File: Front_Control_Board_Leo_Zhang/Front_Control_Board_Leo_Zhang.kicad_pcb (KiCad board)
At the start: 2 copper layers, 110 parts, among them J1 22035035, J10 430450200, J11 430450200, J12 430450200, J13 22035035, J14 M22-7130442, J2 Molex Micro-Fit 4 Pin, J3 430450200, J4 430450200, J5 430450200, J6 430450200, J7 22035035, J8 22035035, J9 22035035, Q1 PSMN5R2-60YL, Q2 PSMN5R2-60YL, Q3 PSMN5R2-60YL, Q4 PSMN5R2-60YL, Q5 PSMN5R2-60YL, Q6 PSMN5R2-60YL, U2 ADS1118IDGS, U3 MCP2562-E-P, U4 MCP6286T-E/OT, U5 UA78M05QDCYRG4Q1, U6 MCP6286T-E/OT, U7 MCP6286T-E/OT

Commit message: Done w first draft! waiting for feedback
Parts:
- removed D2, D3: PTVS12VZ1USK, Diode_SMD:Nexperia_DSN1608-2_1.6x0.8mm
- added J15: M22-7130442, SMV_Connectors:M22-7130442_TYC, F.Cu at (247.5, 45.0)
- added TP37: BlinkRSig, TestPoint:TestPoint_Pad_D1.0mm, F.Cu at (249.5, 67.8)
- added TP38: HLRSig, TestPoint:TestPoint_Pad_D1.0mm, F.Cu at (250.0, 61.2)
- added TP39: HLLSig, TestPoint:TestPoint_Pad_D1.0mm, F.Cu at (251.5, 55.0)
- added TP40: HornSig, TestPoint:TestPoint_Pad_D1.0mm, F.Cu at (247.8, 56.2)
- J14: footprint Jumperz:M22-7130442_TYC -> SMV_Connectors:M22-7130442_TYC
- TP1: value TestPoint -> BlinkLSig
- TP16: value BlinkR_MOS_G -> BlinkL_MOS_G
- TP17: value Pressure -> Accelerator
- TP7: value Pressure -> Brake
- U3: footprint Package_DIP:DIP-8_W7.62mm -> Package_DIP:SMDIP-8_W7.62mm
- moved J6 243.4 mm to (273.8, 105.4)
- moved J3 203.6 mm to (270.5, 22.2), turned to 90 degrees
- moved J5 196.9 mm to (151.0, 27.3), turned to 180 degrees
- moved J4 182.0 mm to (270.2, 48.5), turned to 90 degrees
- moved J12 154.5 mm to (270.2, 34.5), turned to 90 degrees
- moved J10 153.2 mm to (270.2, 72.0), turned to 90 degrees
- moved J11 144.8 mm to (270.2, 60.0), turned to 90 degrees
- moved U1 127.3 mm to (210.6, 59.2)
- moved TP12 126.6 mm to (259.5, 19.5), turned to -90 degrees
- moved Q1 125.9 mm to (261.6, 24.6), turned to -90 degrees
- moved Q4 125.0 mm to (260.4, 36.5), turned to -90 degrees
- moved J14 122.4 mm to (230.0, 102.9)
- moved TP22 121.0 mm to (265.2, 20.2), turned to 180 degrees
- moved Q5 119.7 mm to (260.3, 50.5), turned to -90 degrees
- moved TP4 117.0 mm to (257.8, 26.8), turned to -90 degrees
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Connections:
- J14 pad 1: (no net) -> /CAN_RX/Jump
- J14 pad 2: (no net) -> unconnected-(J14-A2-Pad2)
- J14 pad 3: (no net) -> unconnected-(J14-A3-Pad3)
- J14 pad 4: (no net) -> /CAN_TX/Jump
- R20 pad 2: Net-(U1-CN7_33) -> Net-(U1-VBAT)
- TP1 pad 1: unconnected-(TP1-Pad1) -> /BlinkLeft/STM32
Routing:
- net +3V3: track 0.00 -> 185.3 mm
- net /Pressure/VFin: track 0.00 -> 124.4 mm
- net /Brake(Hall)/VFin: track 0.00 -> 93.8 mm
- net /Accelerator(Hall)/VFin: track 0.00 -> 63.2 mm
- net GND: track 0.00 -> 62.0 mm, vias 0 -> 26
- net +5V: track 0.00 -> 53.7 mm
- net /Horn/STM32: track 0.00 -> 48.9 mm
- net /CANH: track 0.00 -> 41.6 mm
- net /CANL: track 0.00 -> 41.5 mm
- net /HLL/STM32: track 0.00 -> 39.7 mm
- net /PA8_D7_Standby: track 0.00 -> 37.6 mm
- net /Brake(Hall)/VFout: track 0.00 -> 30.9 mm
- net /D0/Wiper4: track 0.00 -> 30.0 mm
- net /Accelerator(Hall)/VFout: track 0.00 -> 29.8 mm
- net /HLR/STM32: track 0.00 -> 29.6 mm
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- added copper zone on F.Cu, net +12V
- added copper zone on F.Cu, net +5V
- added copper zone on B.Cu, net GND
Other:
- board outline added: 136.5 x 105.5 mm
- board text added: "BlinkL"
- board text added: "BlinkR"
- board text added: "HLL"
- board text added: "HLR"
- board text added: "Horn"
- board text added: "Wiper"

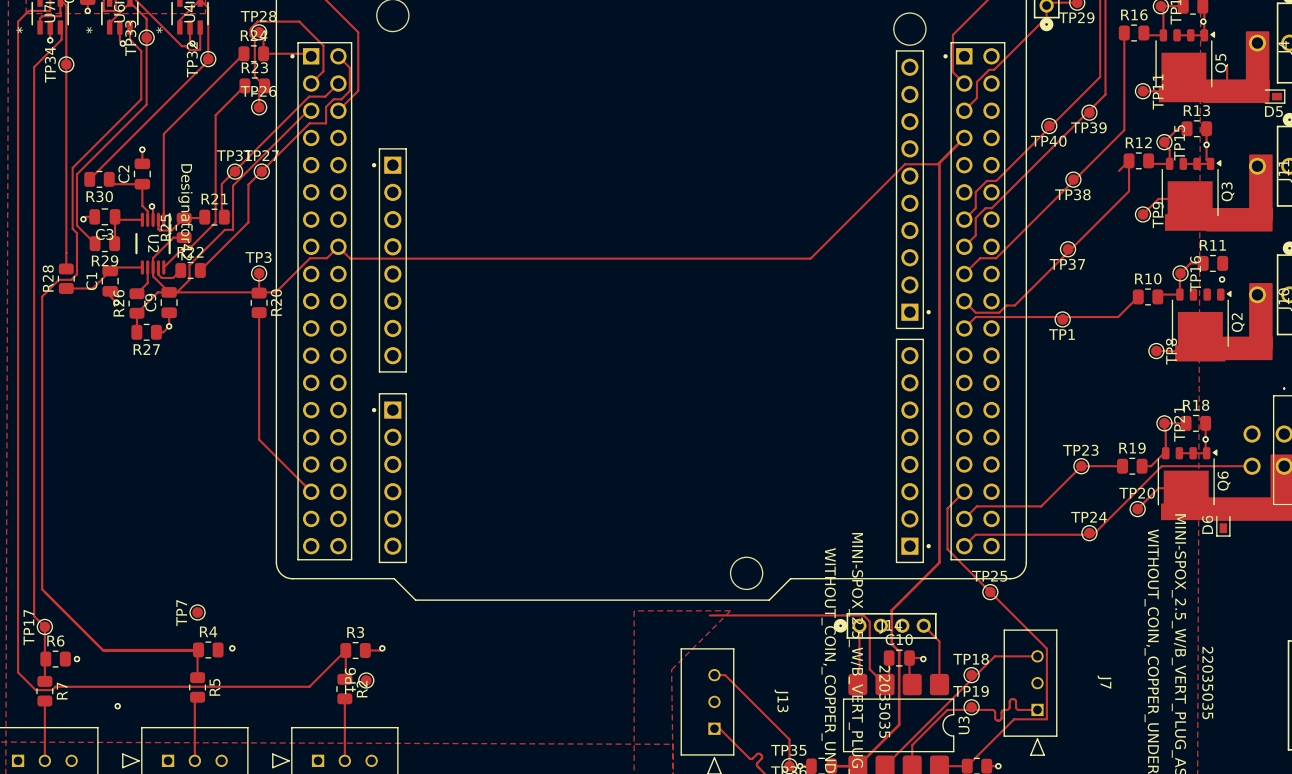
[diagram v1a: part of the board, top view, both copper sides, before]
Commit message: fixed some minor things, unconnected vias and test points
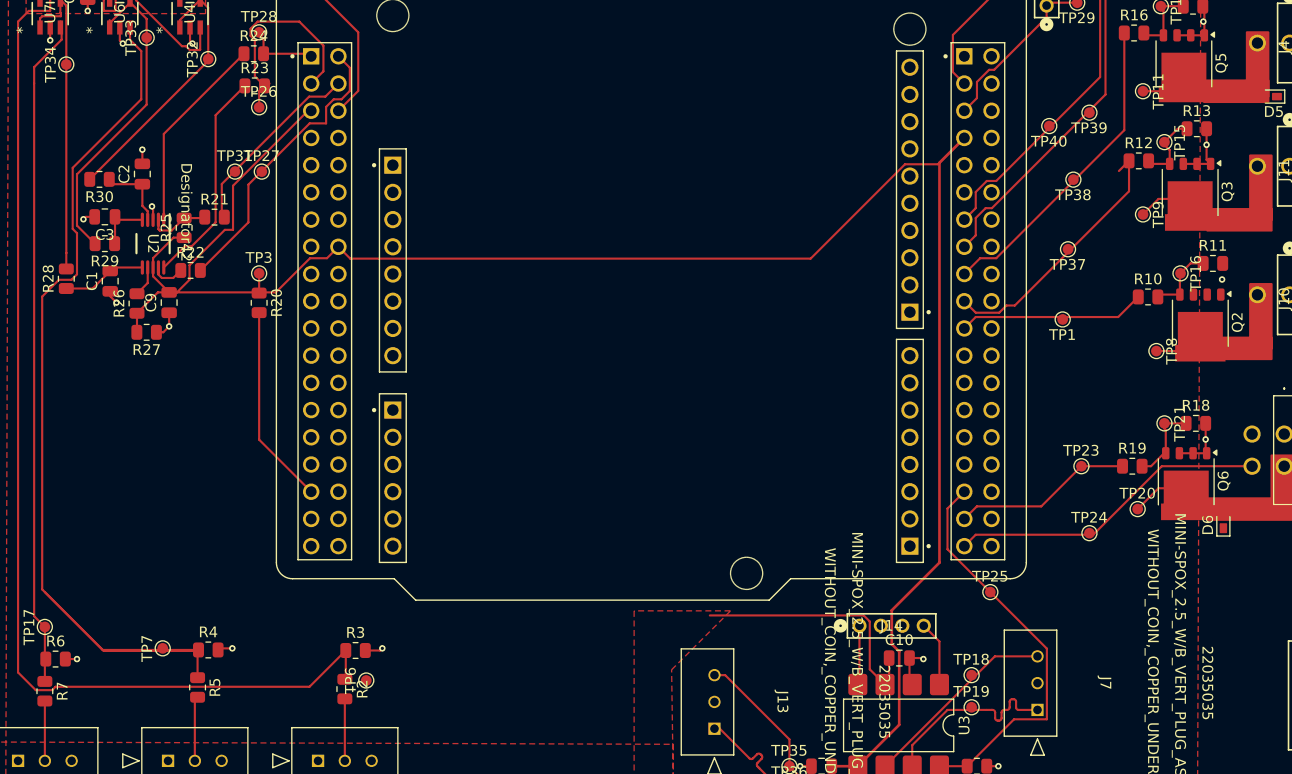
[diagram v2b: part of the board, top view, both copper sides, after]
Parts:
- moved TP7 4.67 mm to (165.0, 105.0)
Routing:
- net GND: track 62.0 -> 64.5 mm, vias 26 -> 25
- net Net-(D5-A): track 7.68 -> 5.78 mm
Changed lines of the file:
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@@
 	(footprint "TestPoint:TestPoint_Pad_D1.0mm"
 		(layer "F.Cu")
-		(at 168.25401 101.649998 90)
+		(at 165 105 90)
 		(descr "SMD pad as test Point, diameter 1.0mm")
 		(tags "test point SMD pad")
@@
 	)
 	(segment
+		(start 171.5 105)
+		(end 170.316508 105)
+		(width 0.2)
+		(layer "F.Cu")
+		(net 1)
+	)
+	(segment
 		(start 163.95 38.05)
 		(end 164.5 37.5)
@@
 	)
 	(segment
+		(start 157 106)
+		(end 155.9125 106)
+		(width 0.2)
+		(layer "F.Cu")
+		(net 1)
+	)
+	(segment
 		(start 262.3459 86.6911)
 		(end 262.4434 86.7886)
@@
 	)
 	(segment
+		(start 170.316508 105)
+		(end 170.16651 105.149998)
+		(width 0.2)
+		(layer "F.Cu")
+		(net 1)
+	)
+	(segment
 		(start 154.5 47.05)
 		(end 154.5 48.25)
@@
 	)
 	(via
-		(at 160.8 110.4)
-		(size 0.6)
-		(drill 0.3)
-		(layers "F.Cu" "B.Cu")
-		(free yes)
-		(net 1)
-	)
-	(via
 		(at 157 106)
 		(size 0.6)
@@
 	)
 	(segment
-		(start 264.350052 50.5834)
-		(end 264.350052 52.4834)
-		(width 0.2)
-		(layer "F.Cu")
-		(net 10)
-	)
-	(segment
 		(start 258.366652 53)
 		(end 256.5 53)
@@
 		(polygon
 			(pts
-				(xy 144.5 16.5) (xy 283 16) (xy 283 36.75) (xy 144.5 37) (xy 144.5 16.5)
+				(xy 144.5 16.5) (xy 283 16) (xy 283 36.75) (xy 144.5 37)
 			)
 		)

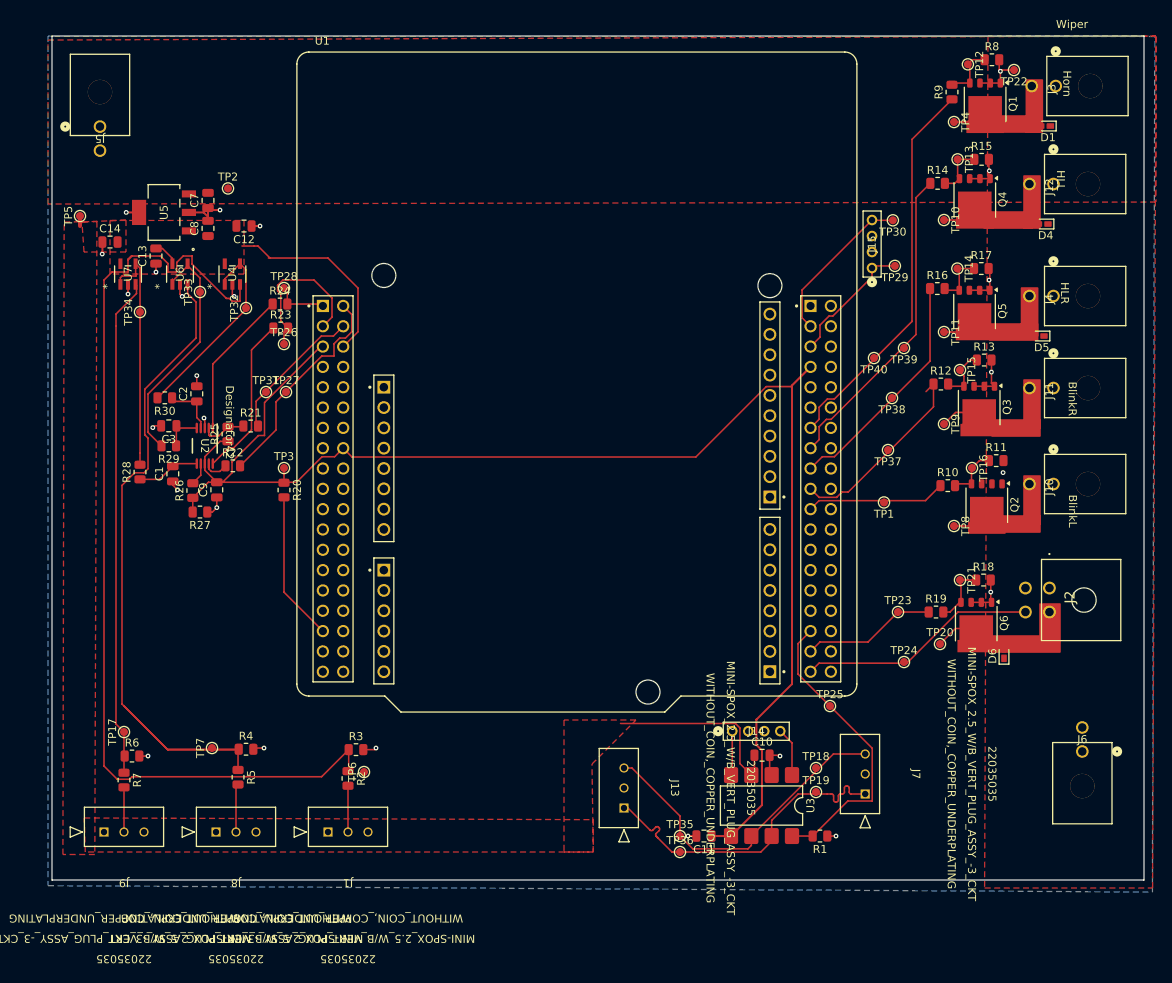
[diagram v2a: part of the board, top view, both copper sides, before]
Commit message: LEDs added, mosfet ground polygons, Ground plane, slight rerouting
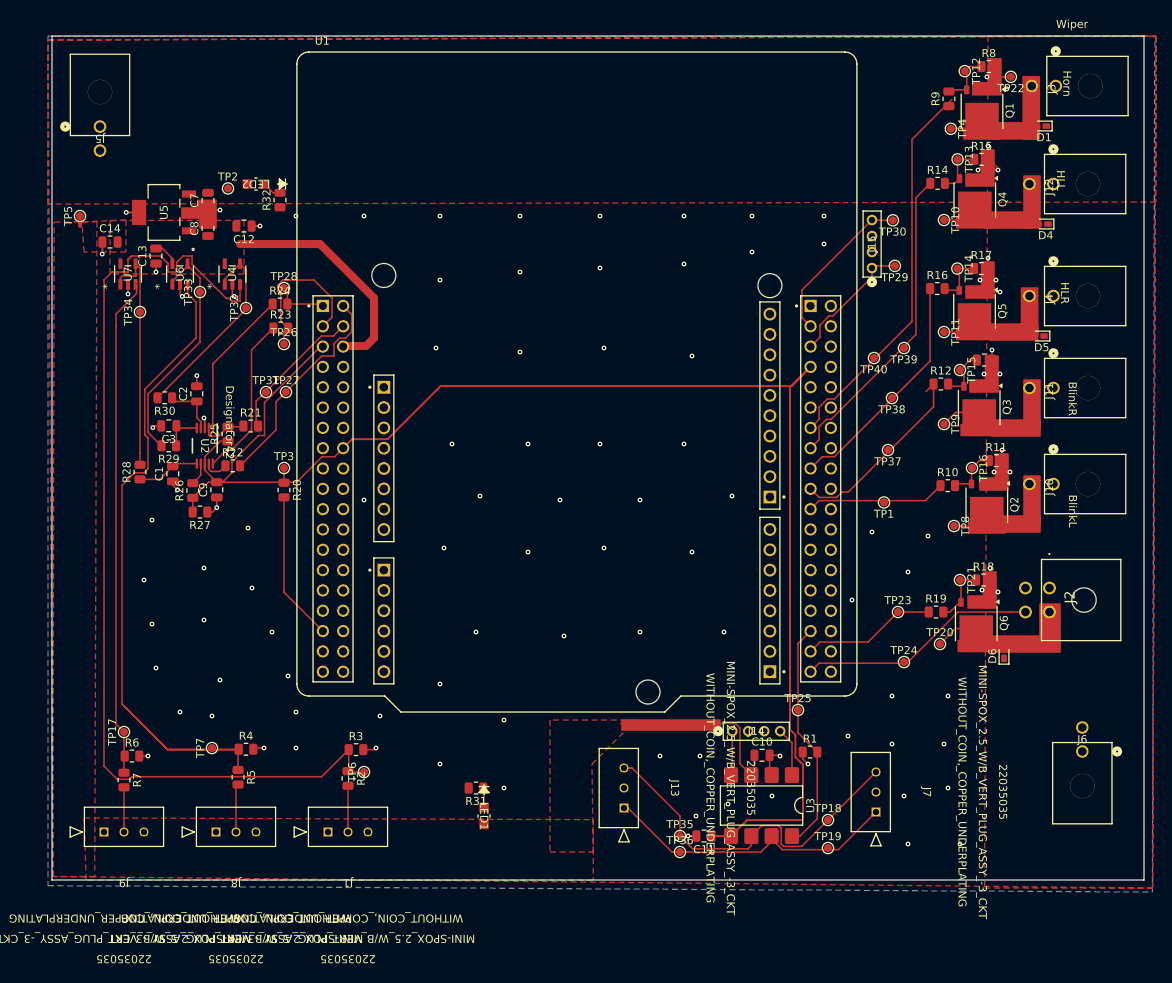
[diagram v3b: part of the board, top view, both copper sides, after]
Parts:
- added LED1: LTST-C170GKT, SMV_Passives:LED_LTST-C170GKT_LTO, F.Cu at (199.0, 113.5)
- added LED2: LTST-C170GKT, SMV_Passives:LED_LTST-C170GKT_LTO, F.Cu at (170.5, 34.5)
- added R31: 200, Resistor_SMD:R_0805_2012Metric, F.Cu at (198.0, 110.0)
- added R32: 1K, Resistor_SMD:R_0805_2012Metric, F.Cu at (173.5, 36.5)
- moved R1 10.6 mm to (239.8, 105.5), turned to 0 degrees
- moved TP19 7.16 mm to (242.0, 117.5)
- moved TP18 6.67 mm to (242.0, 114.0)
- moved TP25 4.03 mm to (238.2, 100.2)
- moved J7 2.63 mm to (248.0, 113.0)
- moved R8 0.93 mm to (262.1, 19.8)
- moved R9 0.93 mm to (257.1, 23.9)
- moved TP22 0.93 mm to (264.9, 21.1)
- moved TP4 0.93 mm to (257.4, 27.6)
- moved Q1 0.93 mm to (261.2, 25.4)
- moved TP12 0.93 mm to (259.1, 20.4)
- moved D1 0.50 mm to (269.0, 27.2)
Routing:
- net GND: track 64.5 -> 91.8 mm, vias 25 -> 110
- net /PA8_D7_Standby: track 37.6 -> 29.2 mm
- net +3V3: track 185.3 -> 189.3 mm
- net +5V: track 53.7 -> 57.6 mm
- net /CANH: track 41.6 -> 37.8 mm
- net /CANL: track 41.5 -> 45.2 mm
- net Net-(LED1-Pad1): track 0.00 -> 2.48 mm
- net Net-(LED2-Pad1): track 0.00 -> 2.40 mm
- net /Pressure/VFin: track 124.4 -> 126.5 mm
- added copper zone on F.Cu, net GND

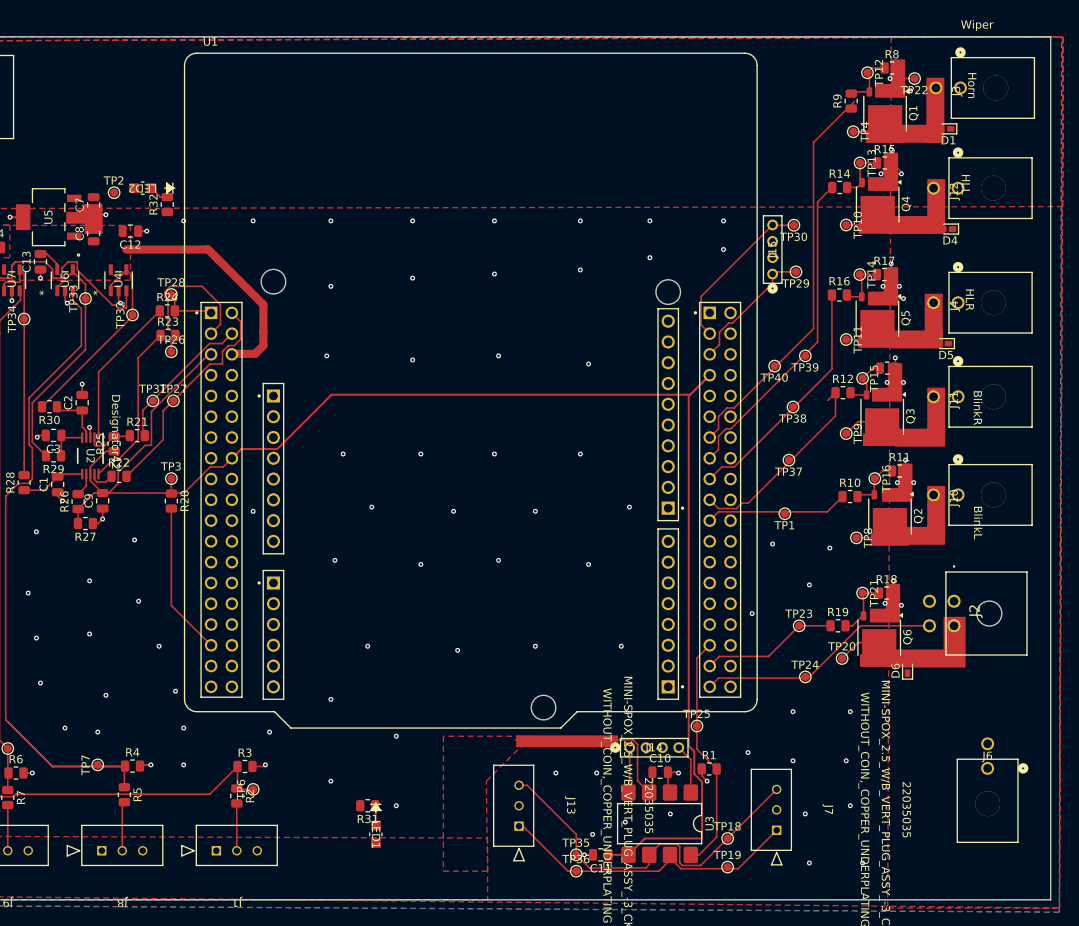
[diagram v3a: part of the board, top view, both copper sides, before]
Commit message: widened 12V plane connect
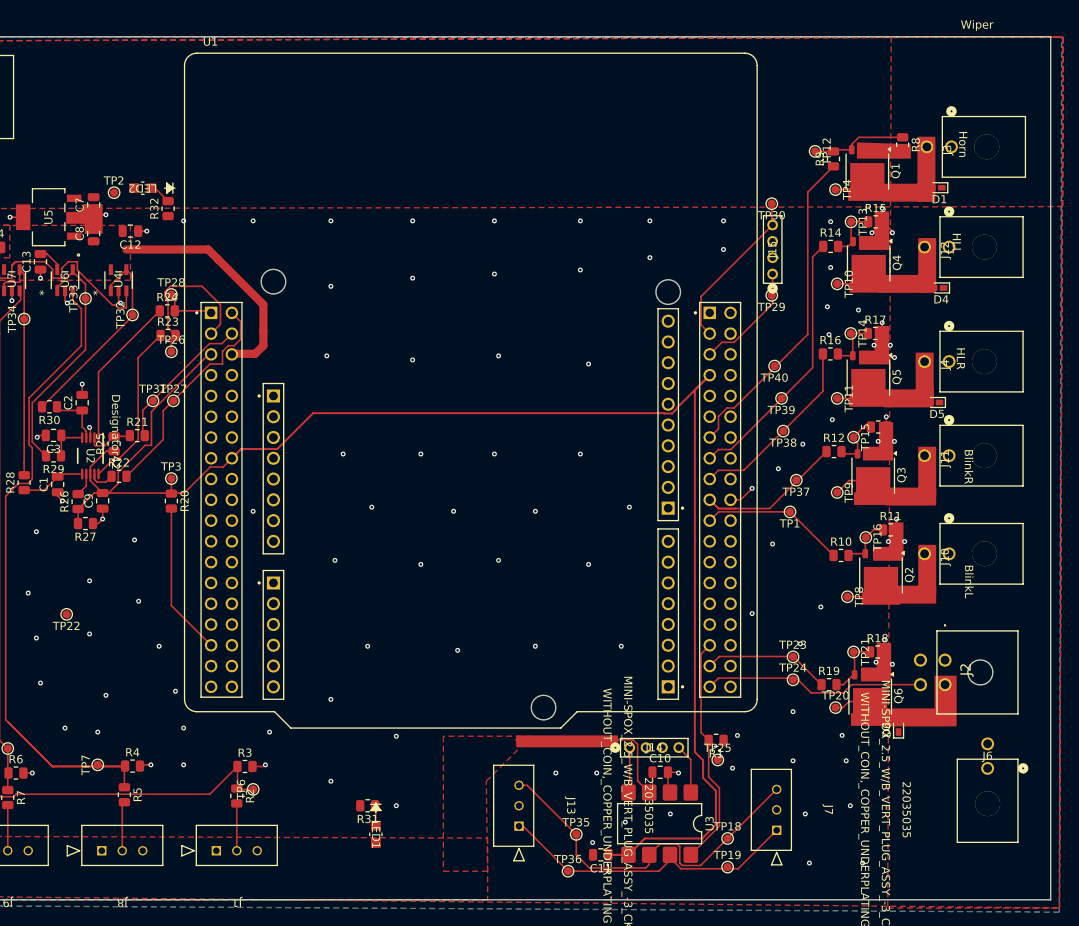
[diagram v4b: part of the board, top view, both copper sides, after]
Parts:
- moved TP22 122.6 mm to (161.2, 86.6)
- moved TP12 11.5 mm to (252.7, 30.0)
- moved R8 9.48 mm to (263.4, 29.2), turned to -90 degrees
- moved Q1 7.40 mm to (259.1, 32.5)
- moved R9 7.40 mm to (254.9, 30.9)
- moved TP4 7.40 mm to (255.2, 34.7)
- moved D1 7.28 mm to (267.9, 34.5)
- moved D6 7.28 mm to (262.9, 100.7)
- moved J10 7.28 mm to (269.1, 79.2)
- moved J11 7.28 mm to (269.1, 67.2)
- moved J12 7.28 mm to (269.1, 41.7)
- moved J2 7.28 mm to (268.6, 92.2)
- moved J4 7.28 mm to (269.1, 55.7)
- moved Q4 7.28 mm to (259.2, 43.7)
- moved R10 7.28 mm to (255.9, 79.4)
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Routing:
- net GND: track 91.8 -> 82.1 mm, vias 110 -> 116
- net /Horn/STM32: track 48.9 -> 39.9 mm
- net /HLL/STM32: track 39.7 -> 32.5 mm
- net /HLR/STM32: track 29.6 -> 22.8 mm
- net Net-(Q1-G): track 7.16 -> 11.9 mm
- net /BlinkRight/STM32: track 24.7 -> 21.3 mm
- net /D0/Wiper4: track 30.0 -> 27.4 mm
- net /CAN_TX: track 16.2 -> 14.3 mm
- net /D1/Wiper2: track 16.8 -> 15.6 mm
- net +3V3: track 189.3 -> 190.1 mm
- net Net-(D6-A): track 6.70 -> 5.91 mm
- net /PA8_D7_Standby: track 29.2 -> 28.4 mm

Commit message: made a few layout changes
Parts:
- LED1, LED2: footprint SMV_Passives:LED_LTST-C170GKT_LTO -> Personal:LED_LTST-C170GKT_LTO
- moved TP5 2.50 mm to (147.8, 40.9)
- moved TP34 2.02 mm to (154.3, 51.6)
- moved TP39 1.03 mm to (249.6, 60.6)
- moved TP25 0.75 mm to (240.1, 104.4)
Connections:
- net /CANH renamed /CAN_P
- net /CANL renamed /CAN_N
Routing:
- net /CAN_P: track 37.8 -> 56.0 mm
- net /CAN_N: track 45.2 -> 55.5 mm
- net /Accelerator(Hall)/VFout: track 29.8 -> 33.4 mm
- net /BlinkRight/STM32: track 21.3 -> 19.3 mm
- net +3V3: track 190.1 -> 188.9 mm
- net +5V: track 57.6 -> 56.3 mm
- net /BlinkLeft/STM32: track 17.8 -> 18.8 mm
- net /HLL/STM32: track 32.5 -> 33.5 mm
- net /Pressure/VFin: track 126.5 -> 127.2 mm
- net /CAN_RX: track 20.0 -> 20.6 mm
- net GND: vias 116 -> 117
